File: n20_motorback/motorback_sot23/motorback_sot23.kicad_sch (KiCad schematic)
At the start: 12 parts, among them J1 Servo wire input, J2 Conn_01x01_Male, J3 Conn_01x01_Male, U1 DRV8837DSGR, U2 ATtiny4-TS, U3 AIC1734-33GUTR

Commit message: motorback sot23 update
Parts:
- added J4: prog_pins, motorback:pogopins_5, symbol Connector:Conn_01x05_Male
- J1: footprint Connector_JST:JST_SH_SM05B-SRSS-TB_1x05-1MP_P1.00mm_Horizontal -> motorback:JST_SH_3or5
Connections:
- net GND: now also J4.1 (Pin_1)
- net MOTORF: now also J4.5 (Pin_5)
- net MOTORR: now also J4.4 (Pin_4)
- net PWMIN: now also J4.3 (Pin_3)
- net VLOGIC: now also J4.2 (Pin_2)
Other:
- note added: "(reset / prog)"
- note added: "PB0/"
- note added: "PB1/"
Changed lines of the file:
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@@
+    (stroke (width 0) (type solid) (color 0 0 0 0))
+  )
+  (wire (pts (xy 36.83 81.28) (xy 45.72 81.28))
+    (stroke (width 0) (type solid) (color 0 0 0 0))
+  )
+  (wire (pts (xy 36.83 83.82) (xy 46.355 83.82))
+    (stroke (width 0) (type solid) (color 0 0 0 0))
+  )
+  (wire (pts (xy 36.83 86.36) (xy 44.45 86.36))
+    (stroke (width 0) (type solid) (color 0 0 0 0))
+  )
+  (wire (pts (xy 36.83 88.9) (xy 44.45 88.9))
+    (stroke (width 0) (type solid) (color 0 0 0 0))
+  )
+  (wire (pts (xy 36.83 91.44) (xy 41.275 91.44))
+    (stroke (width 0) (type solid) (color 0 0 0 0))
+  )
+  (wire (pts (xy 41.275 91.44) (xy 41.275 95.25))
     (stroke (width 0) (type solid) (color 0 0 0 0))
   )
@@
     (stroke (width 0) (type solid) (color 0 0 0 0))
   )
+  (text "PB1/ " (at 53.34 81.28 180)
+    (effects (font (size 1.27 1.27)) (justify right bottom))
+  )
+  (text "PB0/ " (at 53.34 83.82 180)
+    (effects (font (size 1.27 1.27)) (justify right bottom))
+  )
   (text "Input servo connector" (at 55.88 33.02 180)
+    (effects (font (size 1.27 1.27)) (justify right bottom))
+  )
+  (text "(reset / prog)" (at 67.31 86.995 180)
     (effects (font (size 1.27 1.27)) (justify right bottom))
   )
@@
     (effects (font (size 1.27 1.27)) (justify right bottom))
   )
+  (label "VLOGIC" (at 44.45 88.9 180)
+    (effects (font (size 1.27 1.27)) (justify right bottom))
+  )
   (label "MOTORF" (at 45.72 38.1 180)
     (effects (font (size 1.27 1.27)) (justify right bottom))
   )
+  (label "MOTORF" (at 45.72 81.28 180)
+    (effects (font (size 1.27 1.27)) (justify right bottom))
+  )
   (label "MOTORR" (at 46.355 40.64 180)
+    (effects (font (size 1.27 1.27)) (justify right bottom))
+  )
+  (label "MOTORR" (at 46.355 83.82 180)
     (effects (font (size 1.27 1.27)) (justify right bottom))
   )
@@
     (effects (font (size 1.27 1.27)) (justify left))
   )
+  (global_label "PWMIN" (shape input) (at 44.45 86.36 0)    (property "Intersheet References" "${INTERSHEET_REFS}" (id 0) (at -8.89 38.1 0)
+      (effects (font (size 1.27 1.27)) hide)
+    )
+    (effects (font (size 1.27 1.27)) (justify left))
+  )
   (global_label "VBAT" (shape input) (at 66.04 38.1 90)    (property "Intersheet References" "${INTERSHEET_REFS}" (id 0) (at 0 0 0)
       (effects (font (size 1.27 1.27)) hide)
@@
     )
     (property "Datasheet" "" (id 3) (at 34.29 57.785 0)
+      (effects (font (size 1.27 1.27)) hide)
+    )
+  )
+  (symbol (lib_id "power:GND") (at 41.275 95.25 0) (unit 1)
+    (in_bom yes) (on_board yes)
+    (property "Reference" "#PWR01" (id 0) (at 41.275 101.6 0)
+      (effects (font (size 1.27 1.27)) hide)
+    )
+    (property "Value" "GND" (id 1) (at 41.3893 99.5744 0))
+    (property "Footprint" "" (id 2) (at 41.275 95.25 0)
+      (effects (font (size 1.27 1.27)) hide)
+    )
+    (property "Datasheet" "" (id 3) (at 41.275 95.25 0)
       (effects (font (size 1.27 1.27)) hide)
     )
@@
     )
   )
+  (symbol (lib_id "Connector:Conn_01x05_Male") (at 31.75 86.36 0) (mirror x) (unit 1)
+    (in_bom yes) (on_board yes)
+    (property "Reference" "J4" (id 0) (at 34.4424 95.9042 0))
+    (property "Value" "prog_pins" (id 1) (at 34.442 93.606 0))
+    (property "Footprint" "motorback:pogopins_5" (id 2) (at 31.75 86.36 0)
+      (effects (font (size 1.27 1.27)) hide)
+    )
+    (property "Datasheet" "~" (id 3) (at 31.75 86.36 0)
+      (effects (font (size 1.27 1.27)) hide)
+    )
+  )
   (symbol (lib_id "motorback:Conn_01x05_withmechanical") (at 31.75 43.18 0) (mirror x) (unit 1)
     (in_bom yes) (on_board yes)
     (property "Reference" "J1" (id 0) (at 28.0924 39.3892 0))
     (property "Value" "Servo wire input" (id 1) (at 27.457 32.01 0))
-    (property "Footprint" "Connector_JST:JST_SH_SM05B-SRSS-TB_1x05-1MP_P1.00mm_Horizontal" (id 2) (at 31.75 43.18 0)
+    (property "Footprint" "motorback:JST_SH_3or5" (id 2) (at 31.75 43.18 0)
       (effects (font (size 1.27 1.27)) hide)
     )
@@
       (reference "#FLG0102") (unit 1) (value "PWR_FLAG") (footprint "")
     )
+    (path "/0f38a2c8-94e0-4261-91bf-6a18f8b0888a"
+      (reference "#PWR01") (unit 1) (value "GND") (footprint "")
+    )
     (path "/800a6655-3970-4bbf-bbd5-19ec8cc12863"
       (reference "#PWR02") (unit 1) (value "GND") (footprint "")
@@
     )
     (path "/467fc087-e364-41e4-9a8a-5961f20f29a6"
-      (reference "J1") (unit 1) (value "Servo wire input") (footprint "Connector_JST:JST_SH_SM05B-SRSS-TB_1x05-1MP_P1.00mm_Horizontal")
+      (reference "J1") (unit 1) (value "Servo wire input") (footprint "motorback:JST_SH_3or5")
     )
     (path "/532399d3-003d-420e-972c-88889cc1c8f4"
@@
       (reference "J3") (unit 1) (value "Conn_01x01_Male") (footprint "motorback:motorpad")
     )
+    (path "/cd635830-3c79-43f2-afc8-871817f774af"
+      (reference "J4") (unit 1) (value "prog_pins") (footprint "motorback:pogopins_5")
+    )
     (path "/668b33c0-eeaa-4f9d-b177-e9bb894eaa23"

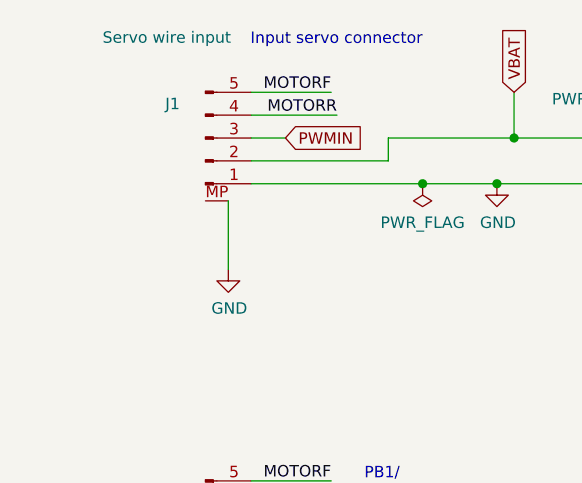
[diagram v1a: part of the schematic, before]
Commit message: More tweaks, use 3-way connector fix 3d models
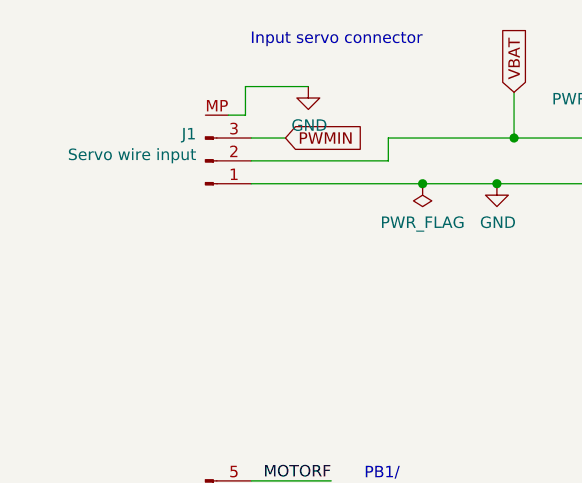
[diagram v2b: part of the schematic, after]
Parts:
- removed J1: Servo wire input, motorback:JST_SH_3or5, symbol motorback:Conn_01x05_withmechanical
- added J1: Servo wire input, Connector_JST:JST_SH_SM03B-SRSS-TB_1x03-1MP_P1.00mm_Horizontal, symbol motorback:Conn_01x03_withmechanical
- C2, C3: LCSC C15849 -> C52923
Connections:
- net GND: now also J1.1 (Pin_1), J1.MP
- net PWMIN: now also J1.3 (Pin_3)
- net VBAT: now also J1.2 (Pin_2)
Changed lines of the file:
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@@
   (junction (at 200.66 63.5) (diameter 1.016) (color 0 0 0 0))
   (junction (at 224.155 58.42) (diameter 1.016) (color 0 0 0 0))
-  (wire (pts (xy 34.29 50.165) (xy 34.29 57.785))
-    (stroke (width 0) (type solid) (color 0 0 0 0))
-  )
-  (wire (pts (xy 36.83 38.1) (xy 45.72 38.1))
-    (stroke (width 0) (type solid) (color 0 0 0 0))
-  )
-  (wire (pts (xy 36.83 40.64) (xy 46.355 40.64))
+  (wire (pts (xy 34.29 40.64) (xy 36.195 40.64))
+    (stroke (width 0) (type solid) (color 0 0 0 0))
+  )
+  (wire (pts (xy 36.195 37.465) (xy 43.18 37.465))
+    (stroke (width 0) (type solid) (color 0 0 0 0))
+  )
+  (wire (pts (xy 36.195 40.64) (xy 36.195 37.465))
     (stroke (width 0) (type solid) (color 0 0 0 0))
   )
@@
     (effects (font (size 1.27 1.27)) (justify right bottom))
   )
-  (label "MOTORF" (at 45.72 38.1 180)
-    (effects (font (size 1.27 1.27)) (justify right bottom))
-  )
   (label "MOTORF" (at 45.72 81.28 180)
-    (effects (font (size 1.27 1.27)) (justify right bottom))
-  )
-  (label "MOTORR" (at 46.355 40.64 180)
     (effects (font (size 1.27 1.27)) (justify right bottom))
   )
@@
     )
   )
-  (symbol (lib_id "power:GND") (at 34.29 57.785 0) (unit 1)
-    (in_bom yes) (on_board yes)
-    (property "Reference" "#PWR0106" (id 0) (at 34.29 64.135 0)
-      (effects (font (size 1.27 1.27)) hide)
-    )
-    (property "Value" "GND" (id 1) (at 34.4043 62.1094 0))
-    (property "Footprint" "" (id 2) (at 34.29 57.785 0)
-      (effects (font (size 1.27 1.27)) hide)
-    )
-    (property "Datasheet" "" (id 3) (at 34.29 57.785 0)
-      (effects (font (size 1.27 1.27)) hide)
-    )
-  )
   (symbol (lib_id "power:GND") (at 41.275 95.25 0) (unit 1)
     (in_bom yes) (on_board yes)
@@
     )
     (property "Datasheet" "" (id 3) (at 41.275 95.25 0)
+      (effects (font (size 1.27 1.27)) hide)
+    )
+  )
+  (symbol (lib_id "power:GND") (at 43.18 37.465 0) (unit 1)
+    (in_bom yes) (on_board yes)
+    (property "Reference" "#PWR0106" (id 0) (at 43.18 43.815 0)
+      (effects (font (size 1.27 1.27)) hide)
+    )
+    (property "Value" "GND" (id 1) (at 43.2943 41.7894 0))
+    (property "Footprint" "" (id 2) (at 43.18 37.465 0)
+      (effects (font (size 1.27 1.27)) hide)
+    )
+    (property "Datasheet" "" (id 3) (at 43.18 37.465 0)
       (effects (font (size 1.27 1.27)) hide)
     )
@@
       (effects (font (size 1.27 1.27)) hide)
     )
-    (property "LCSC" "C15849" (id 4) (at 81.915 46.99 0)
+    (property "LCSC" "C52923" (id 4) (at 81.915 46.99 0)
       (effects (font (size 1.27 1.27)) hide)
     )
@@
       (effects (font (size 1.27 1.27)) hide)
     )
-    (property "LCSC" "C15849" (id 4) (at 114.3 46.99 0)
+    (property "LCSC" "C52923" (id 4) (at 114.3 46.99 0)
       (effects (font (size 1.27 1.27)) hide)
     )
@@
     )
     (property "LCSC" "C19702" (id 4) (at 224.155 62.23 0)
+      (effects (font (size 1.27 1.27)) hide)
+    )
+  )
+  (symbol (lib_id "motorback:Conn_01x03_withmechanical") (at 31.75 45.72 0) (mirror x) (unit 1)
+    (in_bom yes) (on_board yes)
+    (property "Reference" "J1" (id 0) (at 30.7339 42.7418 0)
+      (effects (font (size 1.27 1.27)) (justify right))
+    )
+    (property "Value" "Servo wire input" (id 1) (at 30.734 45.041 0)
+      (effects (font (size 1.27 1.27)) (justify right))
+    )
+    (property "Footprint" "Connector_JST:JST_SH_SM03B-SRSS-TB_1x03-1MP_P1.00mm_Horizontal" (id 2) (at 31.75 45.72 0)
+      (effects (font (size 1.27 1.27)) hide)
+    )
+    (property "Datasheet" "~" (id 3) (at 31.75 45.72 0)
       (effects (font (size 1.27 1.27)) hide)
     )
@@
     )
   )
-  (symbol (lib_id "motorback:Conn_01x05_withmechanical") (at 31.75 43.18 0) (mirror x) (unit 1)
-    (in_bom yes) (on_board yes)
-    (property "Reference" "J1" (id 0) (at 28.0924 39.3892 0))
-    (property "Value" "Servo wire input" (id 1) (at 27.457 32.01 0))
-    (property "Footprint" "motorback:JST_SH_3or5" (id 2) (at 31.75 43.18 0)
-      (effects (font (size 1.27 1.27)) hide)
-    )
-    (property "Datasheet" "~" (id 3) (at 31.75 43.18 0)
-      (effects (font (size 1.27 1.27)) hide)
-    )
-  )
   (symbol (lib_id "motorback:generic_regulator_GOI") (at 101.6 39.37 0) (unit 1)
     (in_bom yes) (on_board yes)
@@
       (reference "D1") (unit 1) (value "LED") (footprint "LED_SMD:LED_0603_1608Metric")
     )
-    (path "/467fc087-e364-41e4-9a8a-5961f20f29a6"
-      (reference "J1") (unit 1) (value "Servo wire input") (footprint "motorback:JST_SH_3or5")
+    (path "/5bb25203-57c0-44b1-b659-12a9e74e5598"
+      (reference "J1") (unit 1) (value "Servo wire input") (footprint "Connector_JST:JST_SH_SM03B-SRSS-TB_1x03-1MP_P1.00mm_Horizontal")
     )
     (path "/532399d3-003d-420e-972c-88889cc1c8f4"

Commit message: motorback updates
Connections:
- net MOTORF: now also J4.4 (Pin_4); no longer J4.5 (Pin_5)
- net MOTORR: now also J4.5 (Pin_5); no longer J4.4 (Pin_4)
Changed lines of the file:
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@@
     (stroke (width 0) (type solid) (color 0 0 0 0))
   )
-  (text "PB1/ " (at 53.34 81.28 180)
+  (text "PB0/ " (at 52.705 81.28 180)
     (effects (font (size 1.27 1.27)) (justify right bottom))
   )
-  (text "PB0/ " (at 53.34 83.82 180)
+  (text "PB1/ " (at 53.975 83.82 180)
     (effects (font (size 1.27 1.27)) (justify right bottom))
   )
@@
     (effects (font (size 1.27 1.27)) (justify right bottom))
   )
-  (label "MOTORF" (at 45.72 81.28 180)
+  (label "MOTORR" (at 45.72 81.28 180)
     (effects (font (size 1.27 1.27)) (justify right bottom))
   )
-  (label "MOTORR" (at 46.355 83.82 180)
+  (label "MOTORF" (at 46.355 83.82 180)
     (effects (font (size 1.27 1.27)) (justify right bottom))
   )
